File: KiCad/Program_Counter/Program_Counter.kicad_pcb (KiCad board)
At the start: 2 copper layers, 190.8 x 160 mm, 28 parts, among them J1 Conn_01x08_Socket, J2 Conn_01x08_Socket, J3 Conn_01x05_Socket, J4 Conn_01x02_Socket, U1 74LS161, U2 74LS161, U3 74LS161, U4 74LS161, U5 74LS245, U6 74LS245

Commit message: finished registier file boards
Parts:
- removed J2: Conn_01x08_Socket, Connector_JST:JST_XH_S8B-XH-A_1x08_P2.50mm_Horizontal
- added H1: MountingHole_Pad, MountingHole:MountingHole_2.2mm_M2_DIN965_Pad, F.Cu at (54.0, 54.0)
- added H2: MountingHole_Pad, MountingHole:MountingHole_2.2mm_M2_DIN965_Pad, F.Cu at (146.0, 54.0)
- added H3: MountingHole_Pad, MountingHole:MountingHole_2.2mm_M2_DIN965_Pad, F.Cu at (54.0, 146.0)
- added H4: MountingHole_Pad, MountingHole:MountingHole_2.2mm_M2_DIN965_Pad, F.Cu at (146.0, 146.0)
- added J5: Conn_01x02_Socket, Connector_JST:JST_XH_S2B-XH-A_1x02_P2.50mm_Horizontal, F.Cu at (71.2, 140.6)
- added J6: Conn_01x03_Socket, Connector_JST:JST_XH_S3B-XH-A-1_1x03_P2.50mm_Horizontal, F.Cu at (82.5, 142.2)
- D0, D1, D10, D11, D12, D13, D14, D15, D2, D3, D4, D5, D6, D7, D8, D9: footprint LED_THT:LED_Rectangular_W5.0mm_H2.0mm_Horizontal_O1.27mm_Z3.0mm -> LED_THT:LED_Rectangular_W3.0mm_H2.0mm
- J3: value Conn_01x05_Socket -> Conn_01x08_Socket; footprint Connector_JST:JST_XH_S5B-XH-A_1x05_P2.50mm_Horizontal -> Connector_JST:JST_XH_S8B-XH-A_1x08_P2.50mm_Horizontal
- moved RN1 220.7 mm to (-40.3, 74.0), turned to 180 degrees
- moved RN2 183.1 mm to (-2.38, 78.0), turned to 180 degrees
- moved D15 134.8 mm to (136.0, 54.0), turned to -90 degrees
- moved D14 132.2 mm to (132.0, 54.0), turned to -90 degrees
- moved D13 129.5 mm to (128.0, 54.0), turned to -90 degrees
- moved D12 126.8 mm to (124.0, 54.0), turned to -90 degrees
- moved D11 124.8 mm to (120.0, 54.0), turned to -90 degrees
- moved J1 122.9 mm to (121.2, 140.6), turned to 0 degrees
- moved D10 122.1 mm to (116.0, 54.0), turned to -90 degrees
- moved D9 119.4 mm to (112.0, 54.0), turned to -90 degrees
- moved J4 119.2 mm to (60.2, 140.6), turned to 0 degrees
- moved D8 116.7 mm to (108.0, 54.0), turned to -90 degrees
- moved D7 114.1 mm to (104.0, 54.0), turned to -90 degrees
- moved D6 111.4 mm to (100.0, 54.0), turned to -90 degrees
- moved D5 109.1 mm to (96.0, 54.0), turned to -90 degrees
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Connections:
- J1 pad 1: /D7 -> /D8
- J1 pad 2: /D6 -> /D9
- J1 pad 3: /D5 -> /D10
- J1 pad 4: /D4 -> /D11
- J1 pad 5: /D3 -> /D12
- J1 pad 6: /D2 -> /D13
- J1 pad 7: /D1 -> /D14
- J1 pad 8: /D0 -> /D15
- J3 pad 1: PC_LOAD -> /D0
- J3 pad 2: PC_INC -> /D1
- J3 pad 3: PC_OUT -> /D2
- J3 pad 4: MR -> /D3
- J3 pad 5: CLK -> /D4
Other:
- board size 190.8 x 160 mm -> 100 x 100 mm

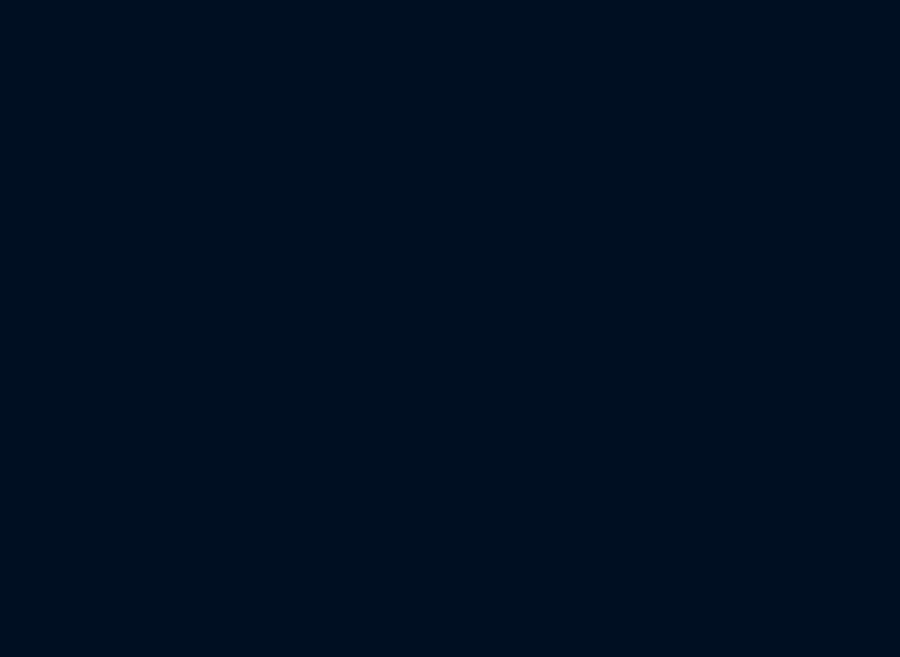
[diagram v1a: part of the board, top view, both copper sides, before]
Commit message: added con_ctrl board mdr_mar
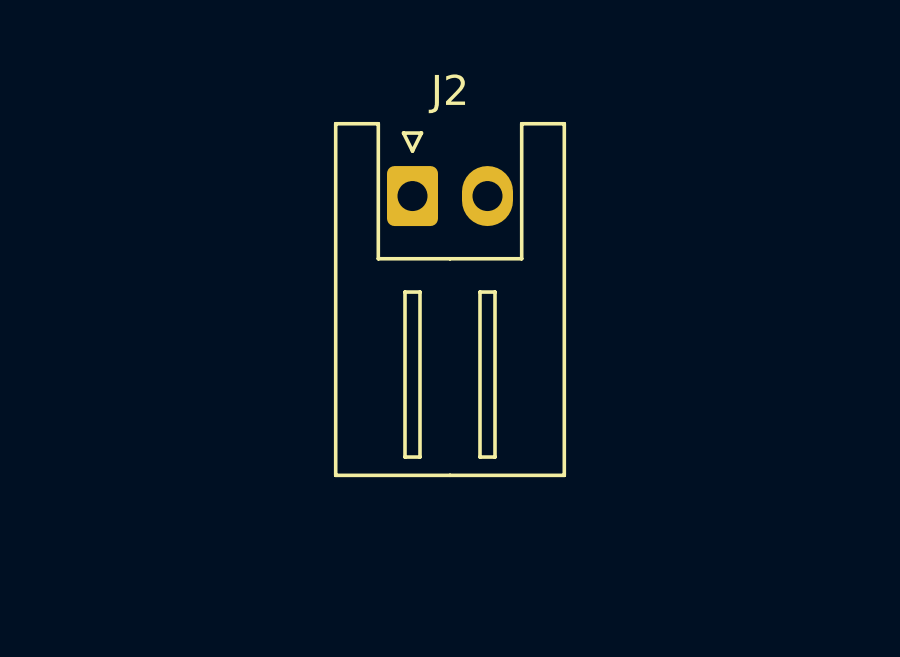
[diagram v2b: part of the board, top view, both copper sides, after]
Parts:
- added J2: Conn_01x02_Socket, Connector_JST:JST_XH_S2B-XH-A_1x02_P2.50mm_Horizontal, F.Cu at (2.98, 2.83)
